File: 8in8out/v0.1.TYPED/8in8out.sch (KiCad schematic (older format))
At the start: 61 parts, among them IC1 ATTINY48-A, J1 RJ45, J2 RJ45, J3 CONN_6, K110 T771D10, K120 T771D10, K130 T771D10, K140 T771D10, K150 T771D10, K160 T771D10, K170 T771D10, K180 T771D10, P1 CONN_5, P100 CONN_2, P101 CONN_2, P102 CONN_2, P103 CONN_2, P105 CONN_2, P106 CONN_2, P110 CONN_2, P120 CONN_2, P130 CONN_2, P140 CONN_2, P150 CONN_2, P160 CONN_2, P170 CONN_2, P180 CONN_2, P2 CONN_5, P3 CONN_10X2, P4 CONN_2, U1 7805, U10 OPTO-TRANSISTOR, U2 ULN2803, U20 OPTO-TRANSISTOR, U30 OPTO-TRANSISTOR, U40 OPTO-TRANSISTOR, U50 OPTO-TRANSISTOR, U60 OPTO-TRANSISTOR, U70 OPTO-TRANSISTOR, U80 OPTO-TRANSISTOR

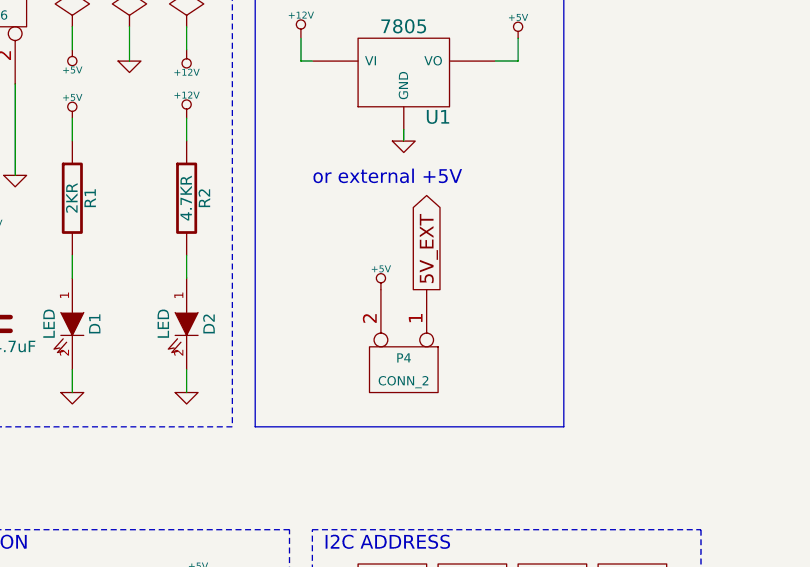
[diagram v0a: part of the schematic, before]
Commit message: elargissement ecartement pads CMS6 reprise plan de masse
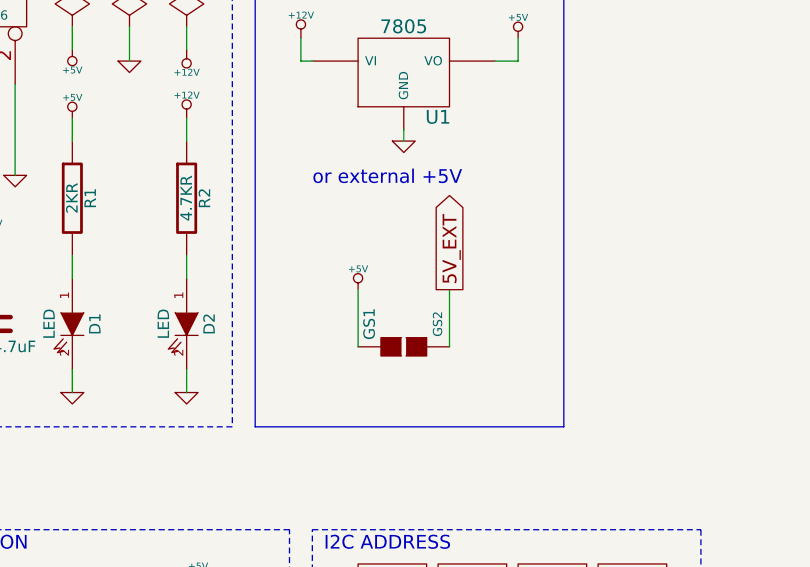
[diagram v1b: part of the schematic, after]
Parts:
- removed P4: CONN_2, symbol CONN_2
- added GS1: GS2, symbol GS2
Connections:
- net +5V: now also GS1.1 (G1)
- net 5V_EXT: now also GS1.2 (G2)
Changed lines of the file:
@@
 	1    0    0    -1
-$EndComp
-$Comp
-L CONN_2 P4
-U 1 1 513A0308
-P 12700 3850
-F 0 "P4" V 12650 3850 40  0000 C CNN
-F 1 "CONN_2" V 12750 3850 40  0000 C CNN
-F 2 "" H 12700 3850 60  0000 C CNN
-F 3 "" H 12700 3850 60  0000 C CNN
-	1    12700 3850
-	0    1    1    0
 $EndComp
 Text GLabel 13450 6750 3    60   Output ~ 0
 5V_EXT
-Text GLabel 12800 3500 1    60   Output ~ 0
+Text GLabel 12900 3500 1    60   Output ~ 0
 5V_EXT
 $Comp
 L +5V #PWR052
 U 1 1 513A033D
-P 12600 3500
-F 0 "#PWR052" H 12600 3590 20  0001 C CNN
-F 1 "+5V" H 12600 3590 30  0000 C CNN
-F 2 "" H 12600 3500 60  0001 C CNN
-F 3 "" H 12600 3500 60  0001 C CNN
-	1    12600 3500
+P 12500 3500
+F 0 "#PWR052" H 12500 3590 20  0001 C CNN
+F 1 "+5V" H 12500 3590 30  0000 C CNN
+F 2 "" H 12500 3500 60  0001 C CNN
+F 3 "" H 12500 3500 60  0001 C CNN
+	1    12500 3500
 	1    0    0    -1
 $EndComp
@@
 Wire Wire Line
 	11800 4850 11800 4800
+$Comp
+L GS2 GS1
+U 1 1 5255B29E
+P 12700 3750
+F 0 "GS1" H 12800 3900 50  0000 C CNN
+F 1 "GS2" H 12800 3601 40  0000 C CNN
+F 2 "" H 12700 3750 60  0000 C CNN
+F 3 "" H 12700 3750 60  0000 C CNN
+	1    12700 3750
+	0    -1   -1   0
+$EndComp
+Wire Wire Line
+	12500 3500 12500 3750
+Wire Wire Line
+	12900 3750 12900 3500
 $EndSCHEMATC
